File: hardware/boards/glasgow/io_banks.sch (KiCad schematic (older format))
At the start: 26 parts, among them J10 Conn_01x03, J4 Conn_01x02, J5 Conn_02x22_Odd_Even, U30 ICE40HX8K-BG121, U32 SN74LVC1T45DRL

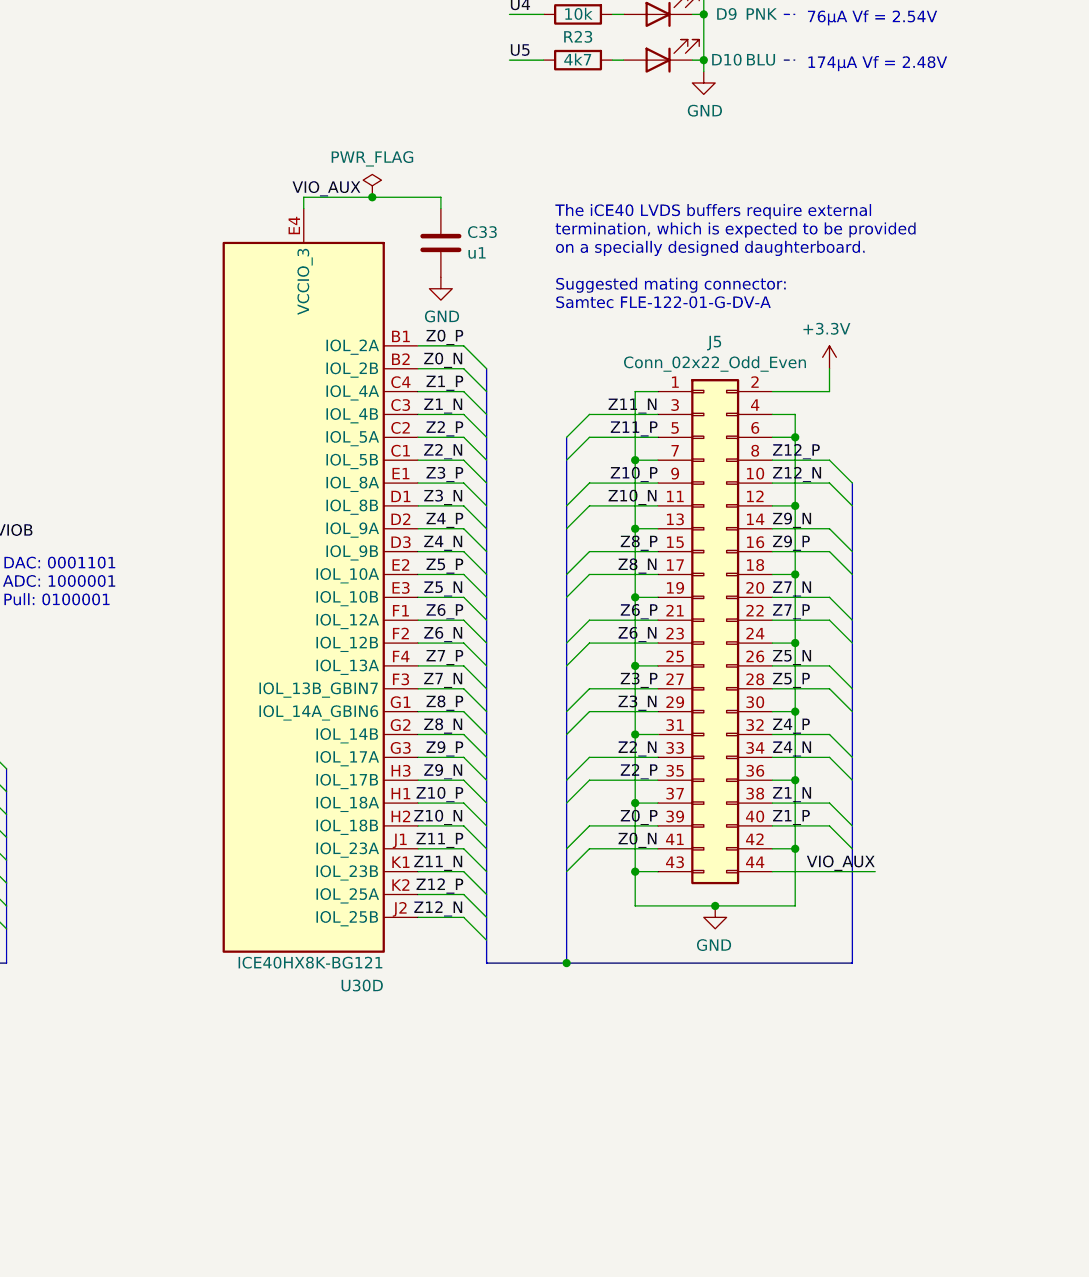
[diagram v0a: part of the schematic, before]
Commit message: revC2: add ESD warning to LVDS connector, add note about it not being available on future revs
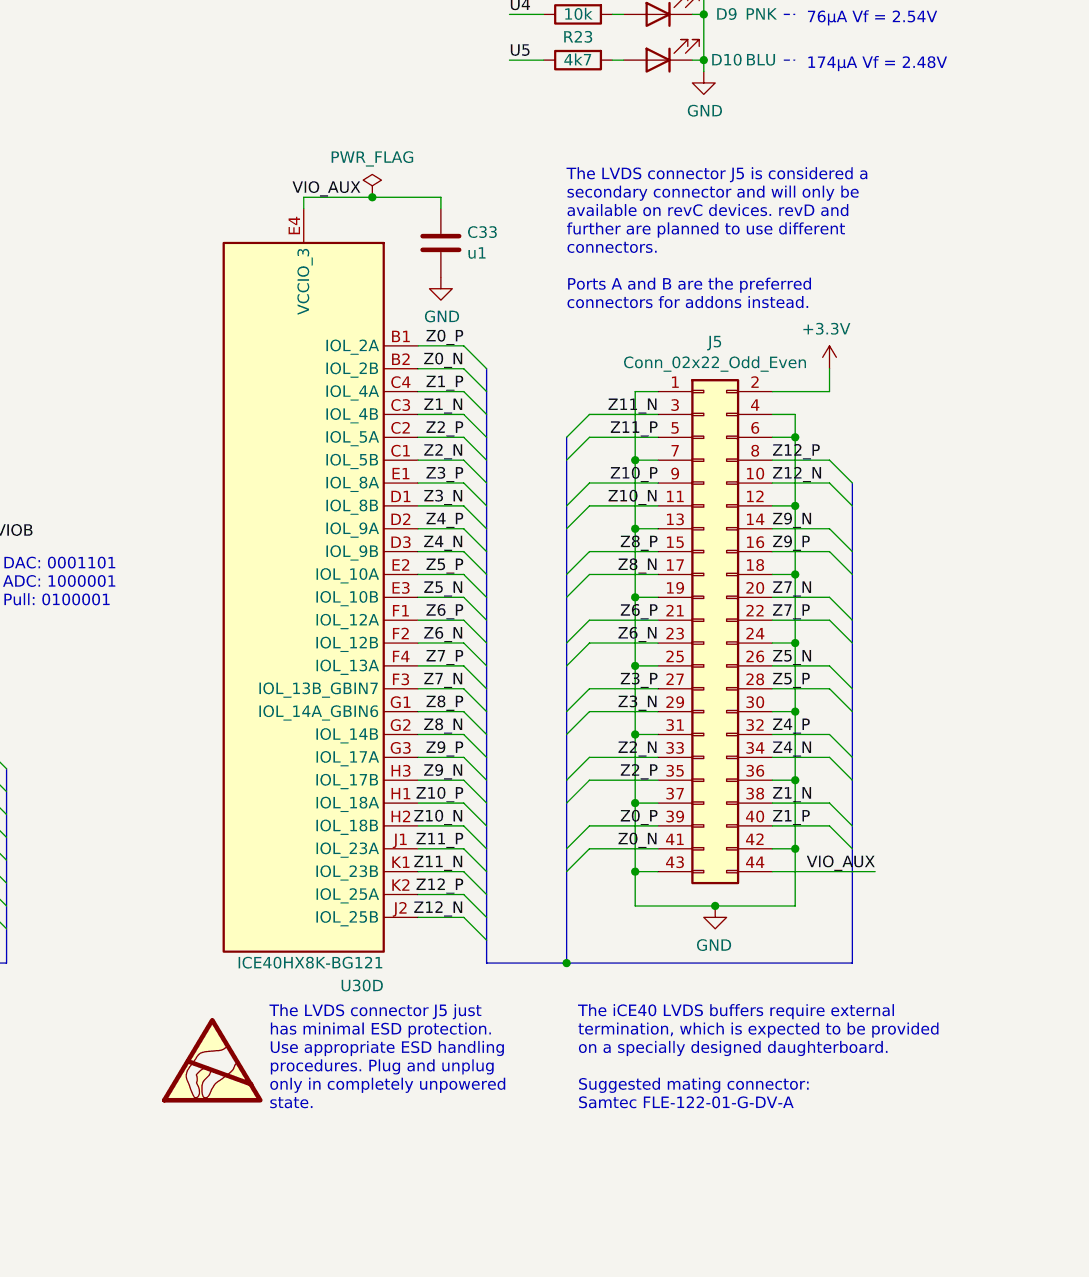
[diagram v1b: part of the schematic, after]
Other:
- note added: "The LVDS connector J5 is considered a \nsecondary connector and will only be \navailable on revC devices. revD and \nfurther are planned to use different \nconnectors.\n\nPorts A and B are the preferred \nconnectors for addons instead.\n"
- note added: "The LVDS connector J5 just \nhas minimal ESD protection.\nUse appropriate ESD handling\nprocedures. Plug and unplug \nonly in completely unpowered \nstate.\n"
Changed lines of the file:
@@
 	-1   0    0    -1
 $EndComp
-Text Notes 9350 2950 0    50   ~ 0
+Text Notes 9450 6450 0    50   ~ 0
 The iCE40 LVDS buffers require external\ntermination, which is expected to be provided\non a specially designed daughterboard.\n\nSuggested mating connector:\nSamtec FLE-122-01-G-DV-A
 Text Notes 900  7150 0    50   ~ 0
@@
 Wire Bus Line
 	9050 3200 9050 5800
+Text Notes 9400 2950 0    50   ~ 0
+The LVDS connector J5 is considered a \nsecondary connector and will only be \navailable on revC devices. revD and \nfurther are planned to use different \nconnectors.\n\nPorts A and B are the preferred \nconnectors for addons instead.\n
+$Comp
+L Graphic:SYM_ESD_Large #SYM?
+U 1 1 5F4FA0F7
+P 7850 6200
+F 0 "#SYM?" H 7850 6400 50  0001 C CNN
+F 1 "SYM_ESD_Large" H 7850 5950 50  0001 C CNN
+F 2 "" H 7845 6170 50  0001 C CNN
+F 3 "~" H 7845 6170 50  0001 C CNN
+	1    7850 6200
+	1    0    0    -1
+$EndComp
+Text Notes 8100 6450 0    50   ~ 0
+The LVDS connector J5 just \nhas minimal ESD protection.\nUse appropriate ESD handling\nprocedures. Plug and unplug \nonly in completely unpowered \nstate.\n
 $EndSCHEMATC

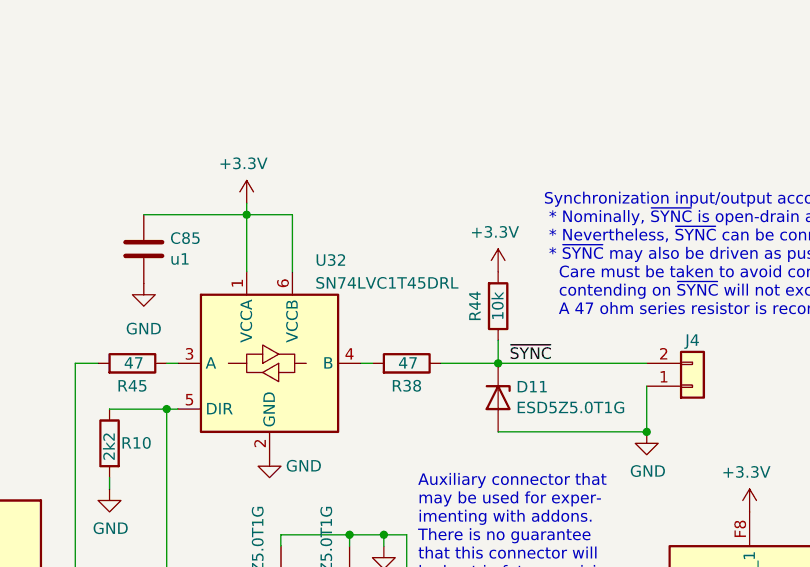
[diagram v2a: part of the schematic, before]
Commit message: revC2: Updated 1b2-bom-keys and corrected levelshifter PN.
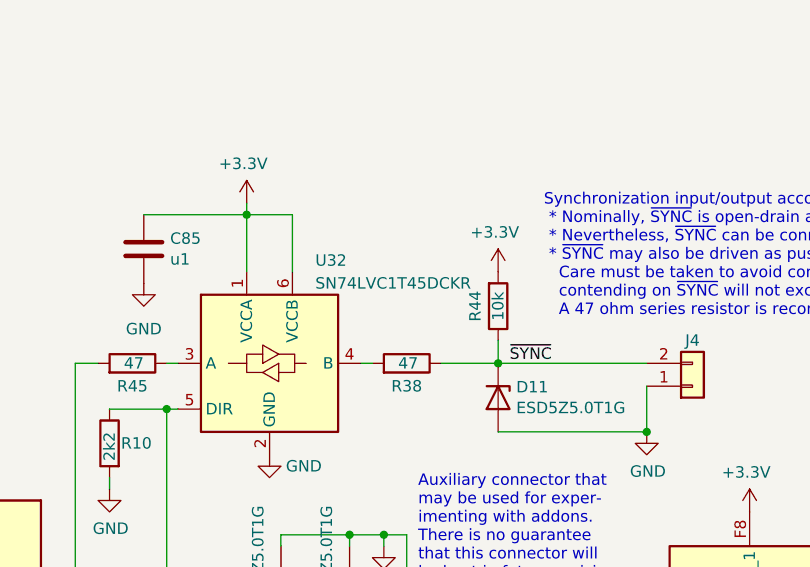
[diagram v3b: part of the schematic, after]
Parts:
- U32: value SN74LVC1T45DRL -> SN74LVC1T45DCKR; 1b2-bom-key ic-sot563-sn74lvc1t45drl -> ic-sot563-sn4lvc1t45dckr
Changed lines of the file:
@@
 P 2650 2400
 F 0 "U32" H 2850 2850 50  0000 L CNN
-F 1 "SN74LVC1T45DRL" H 2850 2750 50  0000 L CNN
+F 1 "SN74LVC1T45DCKR" H 2850 2750 50  0000 L CNN
 F 2 "Glasgow:SOT-363_SC-70-6" H 2650 1950 50  0001 C CNN
 F 3 "http://www.ti.com/lit/ds/symlink/sn74lvc1t45.pdf" H 1750 1750 50  0001 C CNN
 F 4 "Texas Instruments" H 2650 2400 50  0001 C CNN "Mfg"
 F 5 "SN74LVC1T45DRL" H 2650 2400 50  0001 C CNN "MPN"
-F 6 "ic-sot563-sn74lvc1t45drl" H 2650 2400 50  0001 C CNN "1b2-bom-key"
+F 6 "ic-sot563-sn4lvc1t45dckr" H 2650 2400 50  0001 C CNN "1b2-bom-key"
 	1    2650 2400
 	1    0    0    -1
@@
 	0    -1   -1   0
 $EndComp
-Wire Bus Line
-	2400 4950 2400 5800
-Wire Bus Line
-	3450 4950 3450 5800
-Wire Bus Line
-	6950 4950 6950 5800
-Wire Bus Line
-	5850 4950 5850 5800
-Wire Bus Line
-	10650 3700 10650 5800
-Wire Bus Line
-	9400 3500 9400 5800
-Wire Bus Line
-	2050 3850 2050 5800
-Wire Bus Line
-	5500 3750 5500 5800
-Wire Bus Line
-	9050 3200 9050 5800
 Text Notes 9400 2950 0    50   ~ 0
 The LVDS connector J5 is considered a \nsecondary connector and will only be \navailable on revC devices. revD and \nfurther are planned to use different \nconnectors.\n\nPorts A and B are the preferred \nconnectors for addons instead.\n
@@
 Text Notes 8100 6450 0    50   ~ 0
 The LVDS connector J5 just \nhas minimal ESD protection.\nUse appropriate ESD handling\nprocedures. Plug and unplug \nonly in completely unpowered \nstate.\n
+Wire Bus Line
+	2400 4950 2400 5800
+Wire Bus Line
+	3450 4950 3450 5800
+Wire Bus Line
+	6950 4950 6950 5800
+Wire Bus Line
+	5850 4950 5850 5800
+Wire Bus Line
+	10650 3700 10650 5800
+Wire Bus Line
+	9400 3500 9400 5800
+Wire Bus Line
+	2050 3850 2050 5800
+Wire Bus Line
+	5500 3750 5500 5800
+Wire Bus Line
+	9050 3200 9050 5800
 $EndSCHEMATC

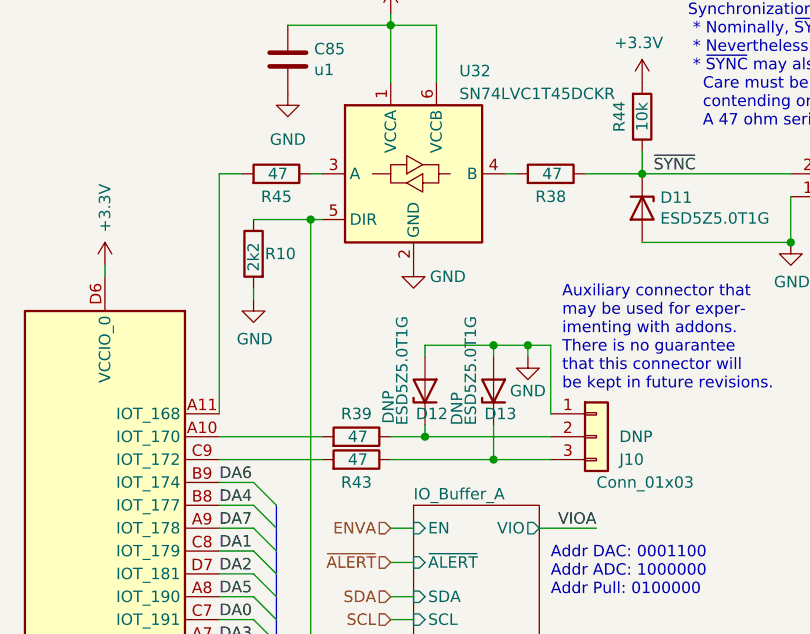
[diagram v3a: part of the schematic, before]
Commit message: revC2: Consolidated sub 1k resistor value notation.
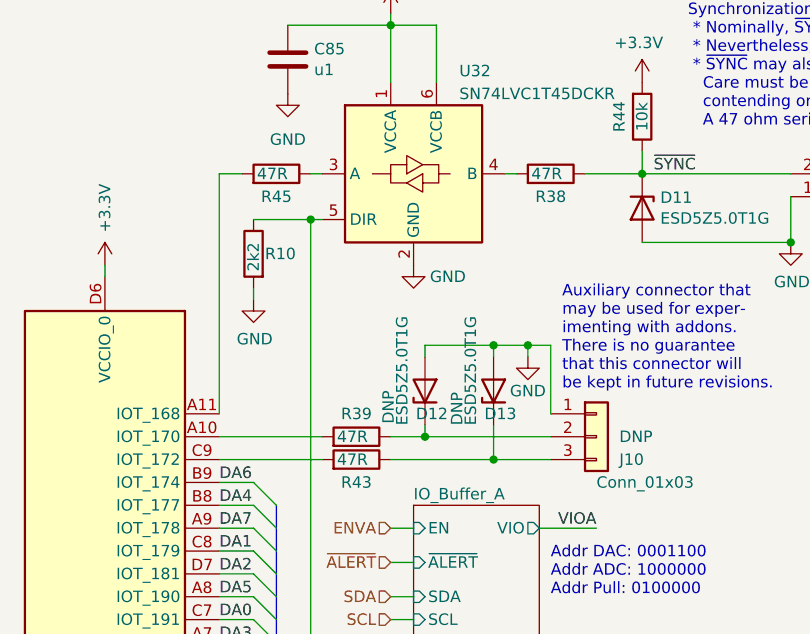
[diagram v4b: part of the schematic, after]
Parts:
- D11: Mfg On Semiconductor -> ON Semiconductor
- R38, R39, R43, R45: value 47 -> 47R; 1b2-bom-key res-0402-47 -> res-0402-47r
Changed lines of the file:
@@
 AR Path="/5C7B59B0/5CBF4EC8" Ref="R38"  Part="1"
 F 0 "R38" V 3150 2400 50  0000 C CNN
-F 1 "47" V 3250 2450 50  0000 R CNN
+F 1 "47R" V 3250 2450 50  0000 R CNN
 F 2 "Resistor_SMD:R_0402_1005Metric" V 3180 2400 50  0001 C CNN
 F 3 "https://www.mouser.com/datasheet/2/447/PYu-RC_Group_51_RoHS_L_10-1527934.pdf" H 3250 2400 50  0001 C CNN
 F 4 "Yageo" H -7100 -150 50  0001 C CNN "Mfg"
 F 5 "RC0402FR-1347RL" H -7100 -150 50  0001 C CNN "MPN"
-F 6 "res-0402-47" H 3250 2400 50  0001 C CNN "1b2-bom-key"
+F 6 "res-0402-47r" H 3250 2400 50  0001 C CNN "1b2-bom-key"
 	1    3250 2400
 	0    1    -1   0
@@
 F 2 "Glasgow:D_SOD-523" H 3650 2550 50  0001 C CNN
 F 3 "https://www.onsemi.com/pub/Collateral/ESD5Z2.5T1-D.PDF" H 3650 2550 50  0001 C CNN
-F 4 "On Semiconductor" H 3650 2550 50  0001 C CNN "Mfg"
+F 4 "ON Semiconductor" H 3650 2550 50  0001 C CNN "Mfg"
 F 5 "ESD5Z5.0T1G" H 3650 2550 50  0001 C CNN "MPN"
 F 6 "esd-diode-sod523-esd5z5_0t1g" H 3650 2550 50  0001 C CNN "1b2-bom-key"
@@
 AR Path="/5C7B59B0/5CB5DA66" Ref="R45"  Part="1"
 F 0 "R45" V 1950 2400 50  0000 C CNN
-F 1 "47" V 2050 2450 50  0000 R CNN
+F 1 "47R" V 2050 2450 50  0000 R CNN
 F 2 "Resistor_SMD:R_0402_1005Metric" V 1980 2400 50  0001 C CNN
 F 3 "https://www.mouser.com/datasheet/2/447/PYu-RC_Group_51_RoHS_L_10-1527934.pdf" H 2050 2400 50  0001 C CNN
 F 4 "Yageo" H -8300 -150 50  0001 C CNN "Mfg"
 F 5 "RC0402FR-1347RL" H -8300 -150 50  0001 C CNN "MPN"
-F 6 "res-0402-47" H 2050 2400 50  0001 C CNN "1b2-bom-key"
+F 6 "res-0402-47r" H 2050 2400 50  0001 C CNN "1b2-bom-key"
 	1    2050 2400
 	0    1    -1   0
@@
 AR Path="/5C7B59B0/5CBF65F8" Ref="R43"  Part="1"
 F 0 "R43" V 2300 3650 50  0000 C CNN
-F 1 "47" V 2400 3700 50  0000 R CNN
+F 1 "47R" V 2400 3700 50  0000 R CNN
 F 2 "Resistor_SMD:R_0402_1005Metric" V 2330 3650 50  0001 C CNN
 F 3 "https://www.mouser.com/datasheet/2/447/PYu-RC_Group_51_RoHS_L_10-1527934.pdf" H 2400 3650 50  0001 C CNN
 F 4 "Yageo" H -7950 1100 50  0001 C CNN "Mfg"
 F 5 "RC0402FR-1347RL" H -7950 1100 50  0001 C CNN "MPN"
-F 6 "res-0402-47" H 2400 3650 50  0001 C CNN "1b2-bom-key"
+F 6 "res-0402-47r" H 2400 3650 50  0001 C CNN "1b2-bom-key"
 	1    2400 3650
 	0    1    -1   0
@@
 AR Path="/5C7B59B0/5CBF658E" Ref="R39"  Part="1"
 F 0 "R39" V 2500 3550 50  0000 C CNN
-F 1 "47" V 2400 3600 50  0000 R CNN
+F 1 "47R" V 2400 3600 50  0000 R CNN
 F 2 "Resistor_SMD:R_0402_1005Metric" V 2330 3550 50  0001 C CNN
 F 3 "https://www.mouser.com/datasheet/2/447/PYu-RC_Group_51_RoHS_L_10-1527934.pdf" H 2400 3550 50  0001 C CNN
 F 4 "Yageo" H -7950 1000 50  0001 C CNN "Mfg"
 F 5 "RC0402FR-1347RL" H -7950 1000 50  0001 C CNN "MPN"
-F 6 "res-0402-47" H 2400 3550 50  0001 C CNN "1b2-bom-key"
+F 6 "res-0402-47r" H 2400 3550 50  0001 C CNN "1b2-bom-key"
 	1    2400 3550
 	0    1    -1   0

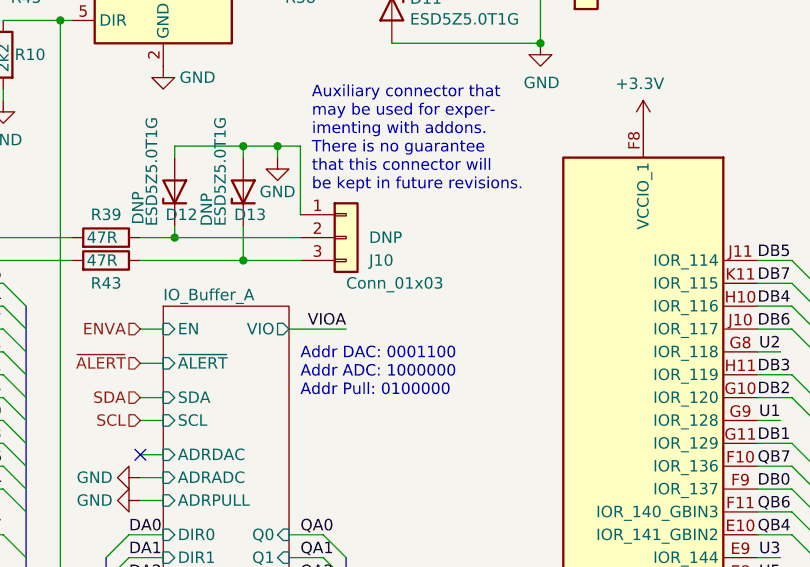
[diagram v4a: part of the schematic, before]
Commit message: revC2: Lots of cleanup to VIO set/sense routing
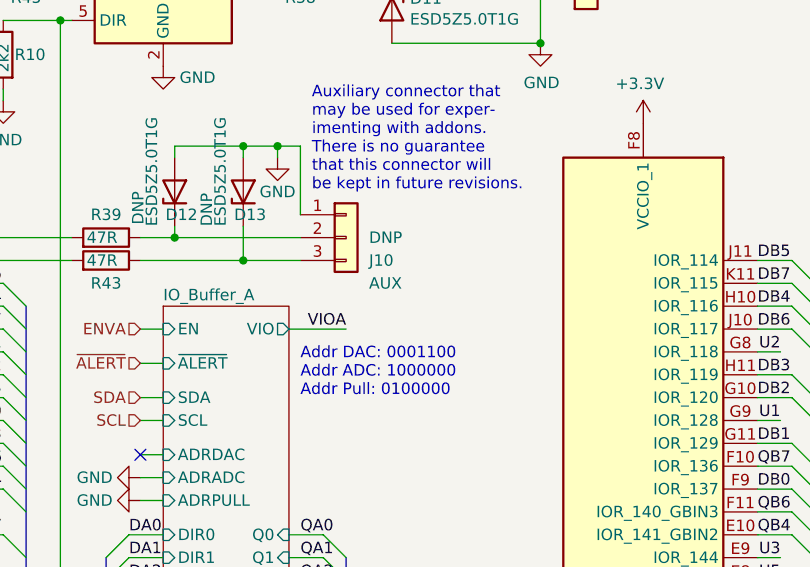
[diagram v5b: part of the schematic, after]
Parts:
- J10: value Conn_01x03 -> AUX
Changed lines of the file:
@@
 P 3450 3550
 F 0 "J10" H 3550 3450 50  0000 L CNN
-F 1 "Conn_01x03" H 3450 3350 50  0000 L CNN
+F 1 "AUX" H 3550 3350 50  0000 L CNN
 F 2 "Connector_PinHeader_2.54mm:PinHeader_1x03_P2.54mm_Vertical" H 3450 3550 50  0001 C CNN
 F 3 "~" H 3450 3550 50  0001 C CNN

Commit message: revC2: Fix review notes
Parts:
- J5: value Conn_02x22_Odd_Even -> PinHeader_2x22_P1.27mm
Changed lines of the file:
@@
 AR Path="/5C7B59B0/5C9E342D" Ref="J5"  Part="1"
 F 0 "J5" H 10050 5517 50  0000 C CNN
-F 1 "Conn_02x22_Odd_Even" H 10050 5426 50  0000 C CNN
+F 1 "PinHeader_2x22_P1.27mm" H 10050 5426 50  0000 C CNN
 F 2 "Glasgow:PinHeader_2x22_P1.27mm_Vertical__SMD" H 10000 4300 50  0001 C CNN
 F 3 "~" H 10000 4300 50  0001 C CNN

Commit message: revC2: fix level shifter MPN
Thanks @gregdavill for spotting & reporting this.
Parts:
- U32: symbol Logic_LevelTranslator:SN74LVC1T45DRL -> Logic_LevelTranslator:SN74LVC1T45DCK; MPN SN74LVC1T45DRL -> SN74LVC1T45DCKR
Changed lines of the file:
@@
 	9150 1050 9300 1050
 $Comp
-L Logic_LevelTranslator:SN74LVC1T45DRL U32
+L Logic_LevelTranslator:SN74LVC1T45DCK U32
 U 1 1 5CA4F297
 P 2650 2400
@@
 F 3 "http://www.ti.com/lit/ds/symlink/sn74lvc1t45.pdf" H 1750 1750 50  0001 C CNN
 F 4 "Texas Instruments" H 2650 2400 50  0001 C CNN "Mfg"
-F 5 "SN74LVC1T45DRL" H 2650 2400 50  0001 C CNN "MPN"
+F 5 "SN74LVC1T45DCKR" H 2650 2400 50  0001 C CNN "MPN"
 F 6 "ic-sot563-sn4lvc1t45dckr" H 2650 2400 50  0001 C CNN "1b2-bom-key"
 	1    2650 2400
